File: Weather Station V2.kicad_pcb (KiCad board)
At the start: 4 copper layers, 123.5 x 67.3 mm, 67 parts, among them J1 SOLAR IN, J10 SP13 Socket, J2 18650, J3 Battery_AUX, J4 Conn_01x08_Socket, J5 Conn_01x08_Socket, J6 USB_C, J7 RYLR998, J8 Breakout, J9 SP13 Socket, Q1 AO4842, Q2 DMP2240UDM-7, Q3 BC547, SW1 LED_ENABLE, SW2 EN/RST, SW3 BOOT, SW4 POWER_SELECT, SW6 POWER, U1 TP4056, U2 DW01A, U3 LDL1117S33R, U4 MT3608, U5 ESP32-S3-WROOM-1U, U7 USBLC6-2SC6

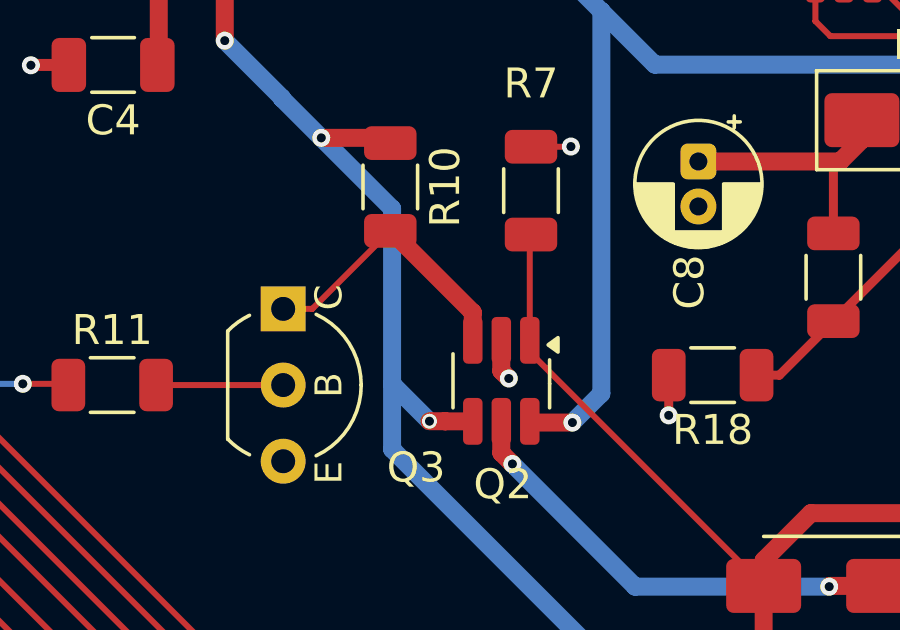
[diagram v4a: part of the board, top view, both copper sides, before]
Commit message: - Changed comment on page 2 - Fixed Q2B PMOS connections (Li mortacci mia!)
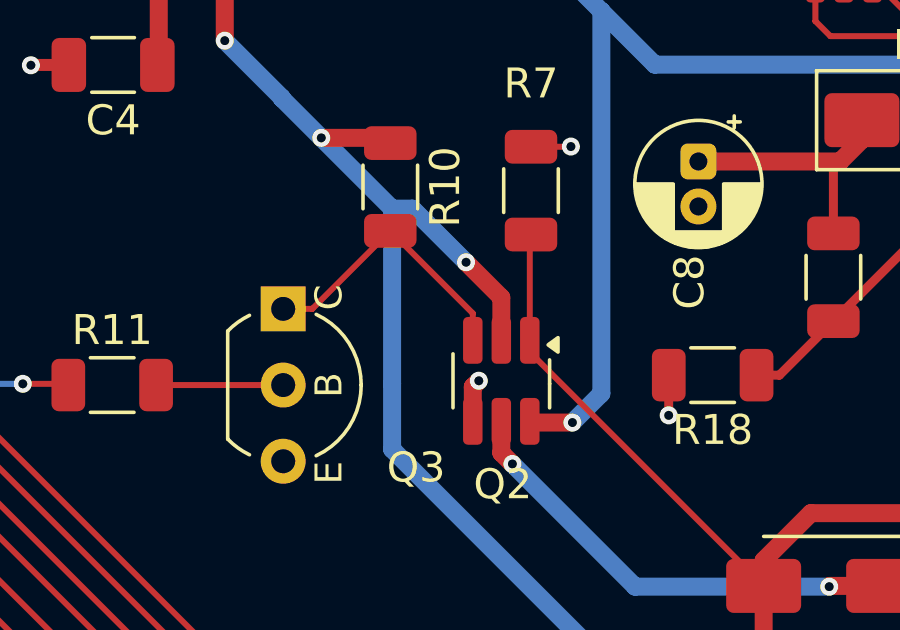
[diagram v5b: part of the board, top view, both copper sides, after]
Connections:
- Q2 pad 2: Net-(D3-K) -> /Battery_SW
- Q2 pad 4: /Battery_SW -> Net-(D3-K)
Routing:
- net /Battery_SW: track 60.6 -> 63.7 mm
- net Net-(D3-K): track 33.8 -> 34.9 mm
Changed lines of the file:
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@@
 			)
 		)
-		(property "Datasheet" "https://www.espressif.com/sites/default/files/documentation/esp32-s3-wroom-1_wroom-1u_datasheet_en.pdf"
+		(property "Datasheet" "${KIPRJMOD}/Data_Sheets/esp32-s3-wroom-1_wroom-1u_datasheet_en.pdf"
 			(at 0 0 90)
 			(unlocked yes)
@@
 			)
 		)
-		(property "Datasheet" "https://cdn.sparkfun.com/assets/home_page_posts/4/4/0/0/Mousebites_Whitepaper_Final.pdf"
+		(property "Datasheet" "${KIPRJMOD}/Data_Sheets/Mousebites_Whitepaper_Final.pdf"
 			(at 0 0 0)
 			(unlocked yes)
@@
 			)
 		)
-		(property "Datasheet" ""
+		(property "Datasheet" "https://www.mouser.it/datasheet/3/175/1/ds31197.pdf"
 			(at 0 0 270)
 			(unlocked yes)
@@
 			(layers "F.Cu" "F.Mask" "F.Paste")
 			(roundrect_rratio 0.25)
-			(net "Net-(D3-K)")
+			(net "/Battery_SW")
 			(pinfunction "S_2")
 			(pintype "passive")
@@
 			(layers "F.Cu" "F.Mask" "F.Paste")
 			(roundrect_rratio 0.25)
-			(net "/Battery_SW")
+			(net "Net-(D3-K)")
 			(pinfunction "D_4")
 			(pintype "passive")
@@
 			)
 		)
-		(property "Datasheet" "https://cdn.sparkfun.com/assets/home_page_posts/4/4/0/0/Mousebites_Whitepaper_Final.pdf"
+		(property "Datasheet" "${KIPRJMOD}/Data_Sheets/Mousebites_Whitepaper_Final.pdf"
 			(at 0 0 0)
 			(unlocked yes)
@@
 			)
 		)
-		(property "Datasheet" "https://www.olimex.com/Products/Breadboarding/BB-PWR-3608/resources/MT3608.pdf"
+		(property "Datasheet" "${KIPRJMOD}/Data_Sheets/MT3608.pdf"
 			(at 0 0 90)
 			(layer "F.Fab")
@@
 			)
 		)
-		(property "Datasheet" "https://www.lcsc.com/datasheet/lcsc_datasheet_2410121619_TOPPOWER-Nanjing-Extension-Microelectronics-TP4056-42-ESOP8_C16581.pdf"
+		(property "Datasheet" "${KIPRJMOD}/Data_Sheets/lcsc_datasheet_2410121619_TOPPOWER-Nanjing-Extension-Microelectronics-TP4056-42-ESOP8_C16581.pdf"
 			(at 0 0 90)
 			(layer "F.Fab")
@@
 			)
 		)
-		(property "Datasheet" "https://cdn.sparkfun.com/assets/home_page_posts/4/4/0/0/Mousebites_Whitepaper_Final.pdf"
+		(property "Datasheet" "${KIPRJMOD}/Data_Sheets/Mousebites_Whitepaper_Final.pdf"
 			(at 0 0 0)
 			(unlocked yes)
@@
 			)
 		)
-		(property "Datasheet" "http://www.mouser.com/ds/2/18/40_c091_abd_e-75918.pdf"
+		(property "Datasheet" "${KIPRJMOD}/Data_Sheets/40_c091_abd_e-75918.pdf"
 			(at 0 0 180)
 			(unlocked yes)
@@
 			)
 		)
-		(property "Datasheet" "https://hmsemi.com/downfile/DW01A.PDF"
+		(property "Datasheet" "${KIPRJMOD}/Data_Sheets/DW01A.PDF"
 			(at 0 0 90)
 			(unlocked yes)
@@
 			)
 		)
-		(property "Datasheet" "https://aosmd.com/sites/default/files/res/data_sheets/AO4842.pdf"
+		(property "Datasheet" "${KIPRJMOD}/Data_Sheets/AO4842.pdf"
 			(at 0 0 90)
 			(layer "F.Fab")
@@
 			)
 		)
-		(property "Datasheet" "https://cdn.sparkfun.com/assets/home_page_posts/4/4/0/0/Mousebites_Whitepaper_Final.pdf"
+		(property "Datasheet" "${KIPRJMOD}/Data_Sheets/Mousebites_Whitepaper_Final.pdf"
 			(at 0 0 0)
 			(unlocked yes)
@@
 			)
 		)
-		(property "Datasheet" "https://www.vishay.com/docs/85816/1n4728a.pdf"
+		(property "Datasheet" "${KIPRJMOD}/Data_Sheets/1n4728a.pdf"
 			(at 0 0 90)
 			(layer "F.Fab")
@@
 			)
 		)
-		(property "Datasheet" "https://www.vishay.com/docs/88751/ss32.pdf"
+		(property "Datasheet" "${KIPRJMOD}/Data_Sheets/ss32.pdf"
 			(at 0 0 0)
 			(unlocked yes)
@@
 			)
 		)
-		(property "Datasheet" "http://www.ti.com/lit/ds/symlink/lm1117.pdf"
+		(property "Datasheet" "${KIPRJMOD}/Data_Sheets/lm1117.pdf"
 			(at 0 0 90)
 			(unlocked yes)
@@
 			)
 		)
-		(property "Datasheet" "https://www.vishay.com/docs/88751/ss32.pdf"
+		(property "Datasheet" "${KIPRJMOD}/Data_Sheets/ss32.pdf"
 			(at 0 0 180)
 			(unlocked yes)
@@
 			)
 		)
-		(property "Datasheet" "https://www.usb.org/sites/default/files/documents/usb_type-c.zip"
+		(property "Datasheet" "${KIPRJMOD}/Data_Sheets/USB_C_Receptacle_USB2.0_16P.pdf"
 			(at 0 0 0)
 			(unlocked yes)
@@
 			)
 		)
-		(property "Datasheet" "https://www.tme.eu/Document/6c5d898a533a0762c2bc33eb26c283a8/BC546-550-DTE.pdf"
+		(property "Datasheet" "${KIPRJMOD}/Data_Sheets/BC546-550-DTE.pdf"
 			(at 0 0 90)
 			(layer "F.Fab")
@@
 			)
 		)
-		(property "Datasheet" "https://cdn.sparkfun.com/assets/home_page_posts/4/4/0/0/Mousebites_Whitepaper_Final.pdf"
+		(property "Datasheet" "${KIPRJMOD}/Data_Sheets/Mousebites_Whitepaper_Final.pdf"
 			(at 0 0 0)
 			(unlocked yes)
@@
 			)
 		)
-		(property "Datasheet" "http://www.mouser.com/ds/2/18/40_c091_abd_e-75918.pdf"
+		(property "Datasheet" "${KIPRJMOD}/Data_Sheets/40_c091_abd_e-75918.pdf"
 			(at 0 0 0)
 			(unlocked yes)
@@
 	)
 	(segment
+		(start 96.3625 77.45)
+		(end 96.1625 77.65)
+		(width 0.6)
+		(layer "F.Cu")
+		(net "Net-(D3-K)")
+	)
+	(segment
 		(start 112.1825 78.885099)
 		(end 112.259901 78.9625)
@@
 	)
 	(segment
-		(start 97.1125 77.1225)
-		(end 97.3625 77.3725)
-		(width 0.6)
-		(layer "F.Cu")
-		(net "Net-(D3-K)")
-	)
-	(segment
 		(start 117.1325 76.2625)
 		(end 117.7825 75.6125)
@@
 	)
 	(segment
-		(start 97.1125 76.1025)
-		(end 97.1125 77.1225)
+		(start 96.1625 77.65)
+		(end 96.1625 78.8025)
 		(width 0.6)
 		(layer "F.Cu")
@@
 	)
 	(via
-		(at 97.3625 77.3725)
+		(at 96.3625 77.45)
 		(size 0.6)
 		(drill 0.3)
@@
 	)
 	(segment
-		(start 97.3625 77.3725)
+		(start 96.3625 77.45)
 		(end 110.0425 77.3725)
 		(width 0.6)
@@
 	)
 	(segment
-		(start 93.4125 72.4525)
-		(end 90.8125 75.0525)
+		(start 96.1625 76.1025)
+		(end 96.1625 75.2025)
 		(width 0.2)
 		(layer "F.Cu")
@@
 	)
 	(segment
-		(start 93.4125 72.4525)
-		(end 93.4425 72.4525)
-		(width 0.6)
+		(start 96.1625 75.2025)
+		(end 93.4125 72.4525)
+		(width 0.2)
 		(layer "F.Cu")
 		(net "Net-(Q2B-G)")
 	)
 	(segment
-		(start 96.1625 75.1725)
-		(end 96.1625 76.1025)
-		(width 0.6)
+		(start 93.4125 72.4525)
+		(end 90.8125 75.0525)
+		(width 0.2)
 		(layer "F.Cu")
 		(net "Net-(Q2B-G)")
 	)
 	(segment
-		(start 93.4425 72.4525)
-		(end 96.1625 75.1725)
+		(start 93.4125 72.4525)
+		(end 93.4425 72.4525)
 		(width 0.6)
 		(layer "F.Cu")
@@
 	)
 	(segment
-		(start 95.2425 78.8025)
-		(end 96.1625 78.8025)
+		(start 95.9375 73.5)
+		(end 97.1125 74.675)
 		(width 0.6)
 		(layer "F.Cu")
@@
 	)
 	(segment
-		(start 95.2375 78.7975)
-		(end 95.2425 78.8025)
+		(start 97.1125 74.675)
+		(end 97.1125 76.1025)
 		(width 0.6)
 		(layer "F.Cu")
@@
 	)
 	(segment
-		(start 94.7175 78.7975)
-		(end 95.2375 78.7975)
-		(width 0.6)
-		(layer "F.Cu")
-		(net "/Battery_SW")
-	)
-	(segment
 		(start 91.1125 69.3525)
 		(end 93.2375 69.3525)
@@
 	)
 	(via
-		(at 94.7175 78.7975)
-		(size 0.5)
-		(drill 0.3)
-		(layers "F.Cu" "B.Cu")
-		(net "/Battery_SW")
-	)
-	(via
 		(at 87.895 66.1125)
 		(size 0.6)
@@
 		(net "/Battery_SW")
 	)
+	(via
+		(at 95.9375 73.5)
+		(size 0.6)
+		(drill 0.3)
+		(layers "F.Cu" "B.Cu")
+		(net "/Battery_SW")
+	)
 	(segment
 		(start 93.4725 79.7325)
@@
 	)
 	(segment
+		(start 94.15 71.7125)
+		(end 95.9375 73.5)
+		(width 0.6)
+		(layer "B.Cu")
+		(net "/Battery_SW")
+	)
+	(segment
 		(start 93.4725 77.5525)
 		(end 93.4725 71.7125)
@@
 	)
 	(segment
-		(start 94.7175 78.7975)
-		(end 93.4725 77.5525)
+		(start 93.4725 71.7125)
+		(end 94.15 71.7125)
 		(width 0.6)
 		(layer "B.Cu")

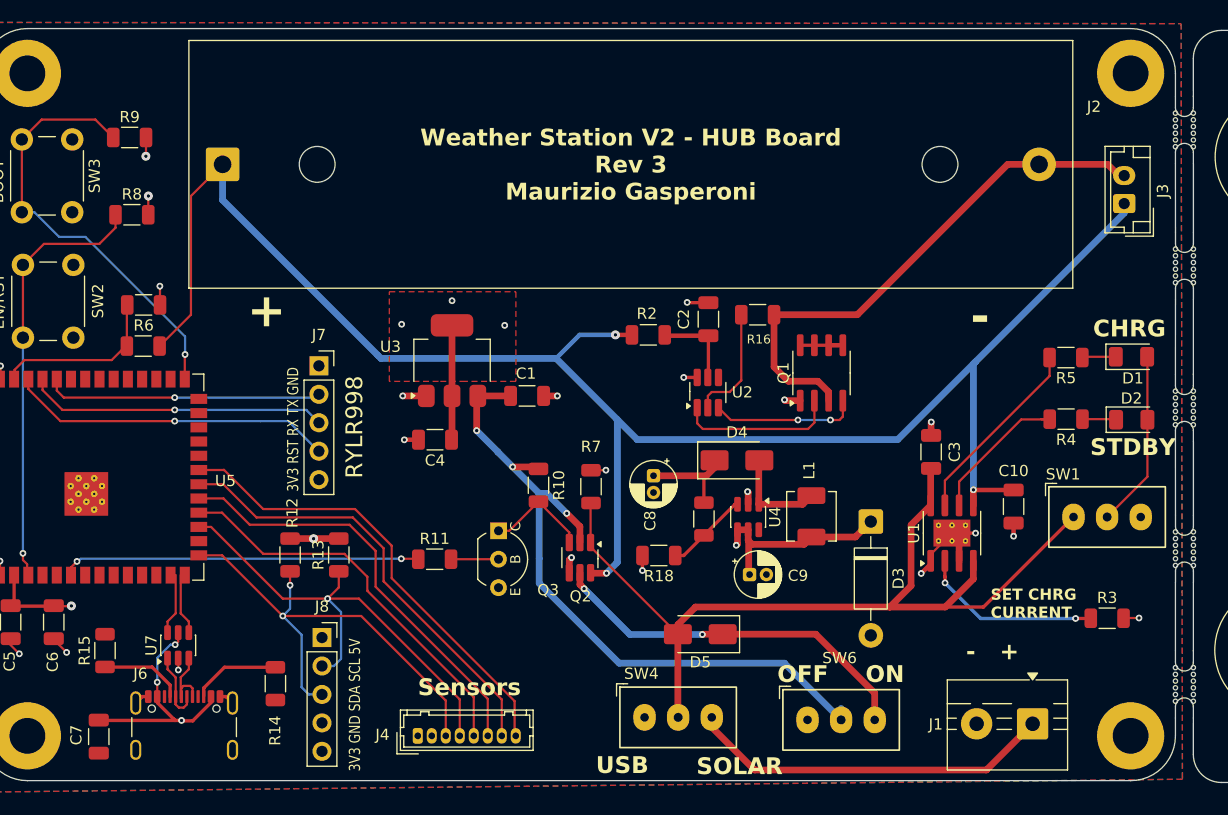
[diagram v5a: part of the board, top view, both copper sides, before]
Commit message: - Fixed SCL SDA swap on breakout pins - Added wind speed test point - Regenerated all boards' stiching vias - Fixed wrong pullup on secondary board WSPEED pin (5V --> 3V3)
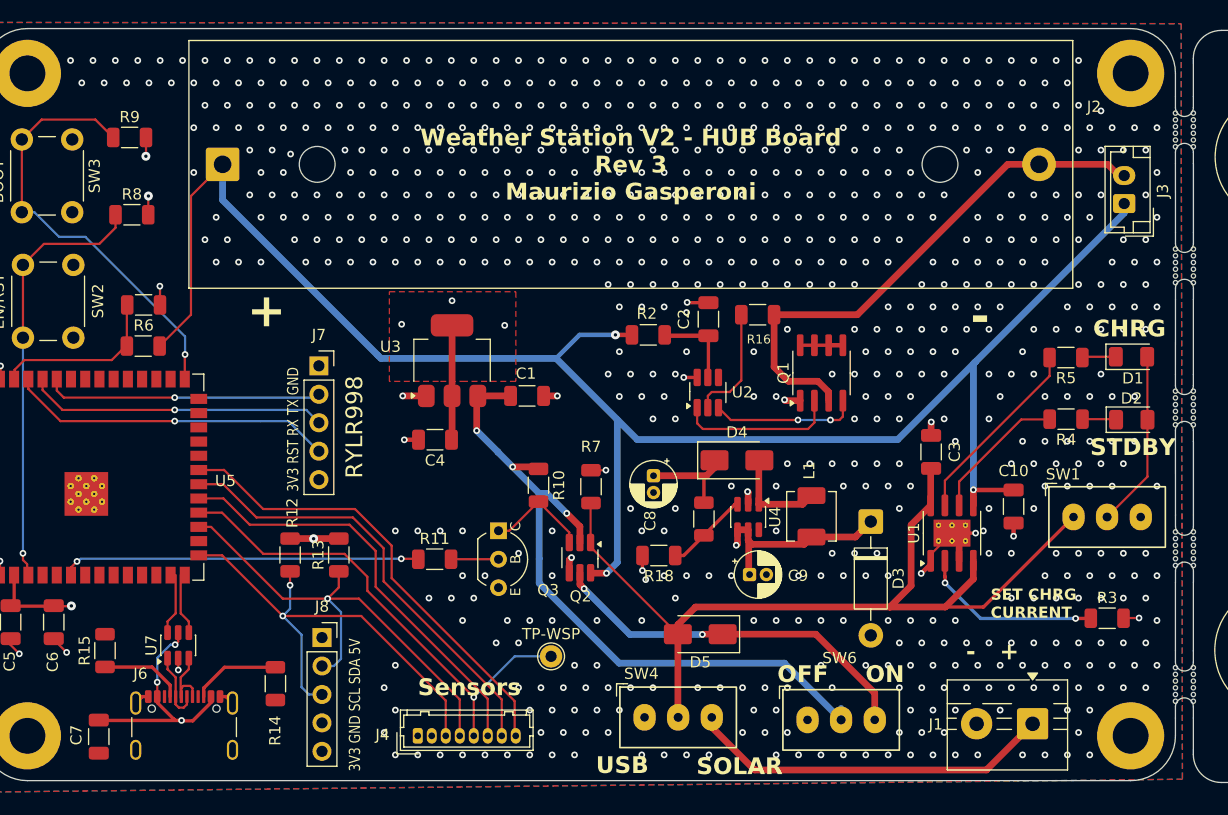
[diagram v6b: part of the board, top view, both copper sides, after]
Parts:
- added TP-WSP: TP-WSPD, TestPoint:TestPoint_THTPad_D2.0mm_Drill1.0mm, F.Cu at (94.5, 86.3)
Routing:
- net /W_SPEED: track 35.6 -> 44.0 mm, vias 0 -> 1
- net Net-(U1-~{STDBY}): track 13.3 -> 12.5 mm
- net GND: vias 20 -> 724
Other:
- board text added: "3V3 GND SCL SDA 5V"
- board text removed: "3V3 GND SDA SCL 5V"

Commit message: Pre-push commit
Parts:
- TP-WSP: footprint TestPoint:TestPoint_THTPad_D2.0mm_Drill1.0mm -> TestPoint_local:TestPoint_THTPad_D2.0mm_Drill1.0mm
